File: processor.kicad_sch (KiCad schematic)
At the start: 84 parts, among them J1 Cartrige, Q1 2N3904, Q2 2N3904, Q3 2N3904, Q4 2N3904, Q5 2N3904, SW1 RESET, U1 68000, U2 27C010, U3 27C010, U39 STB, U4 74HC74, U5 LM555xM, U6 74LS05, Y1 4.433618MHz, Y2 32.084988MHz

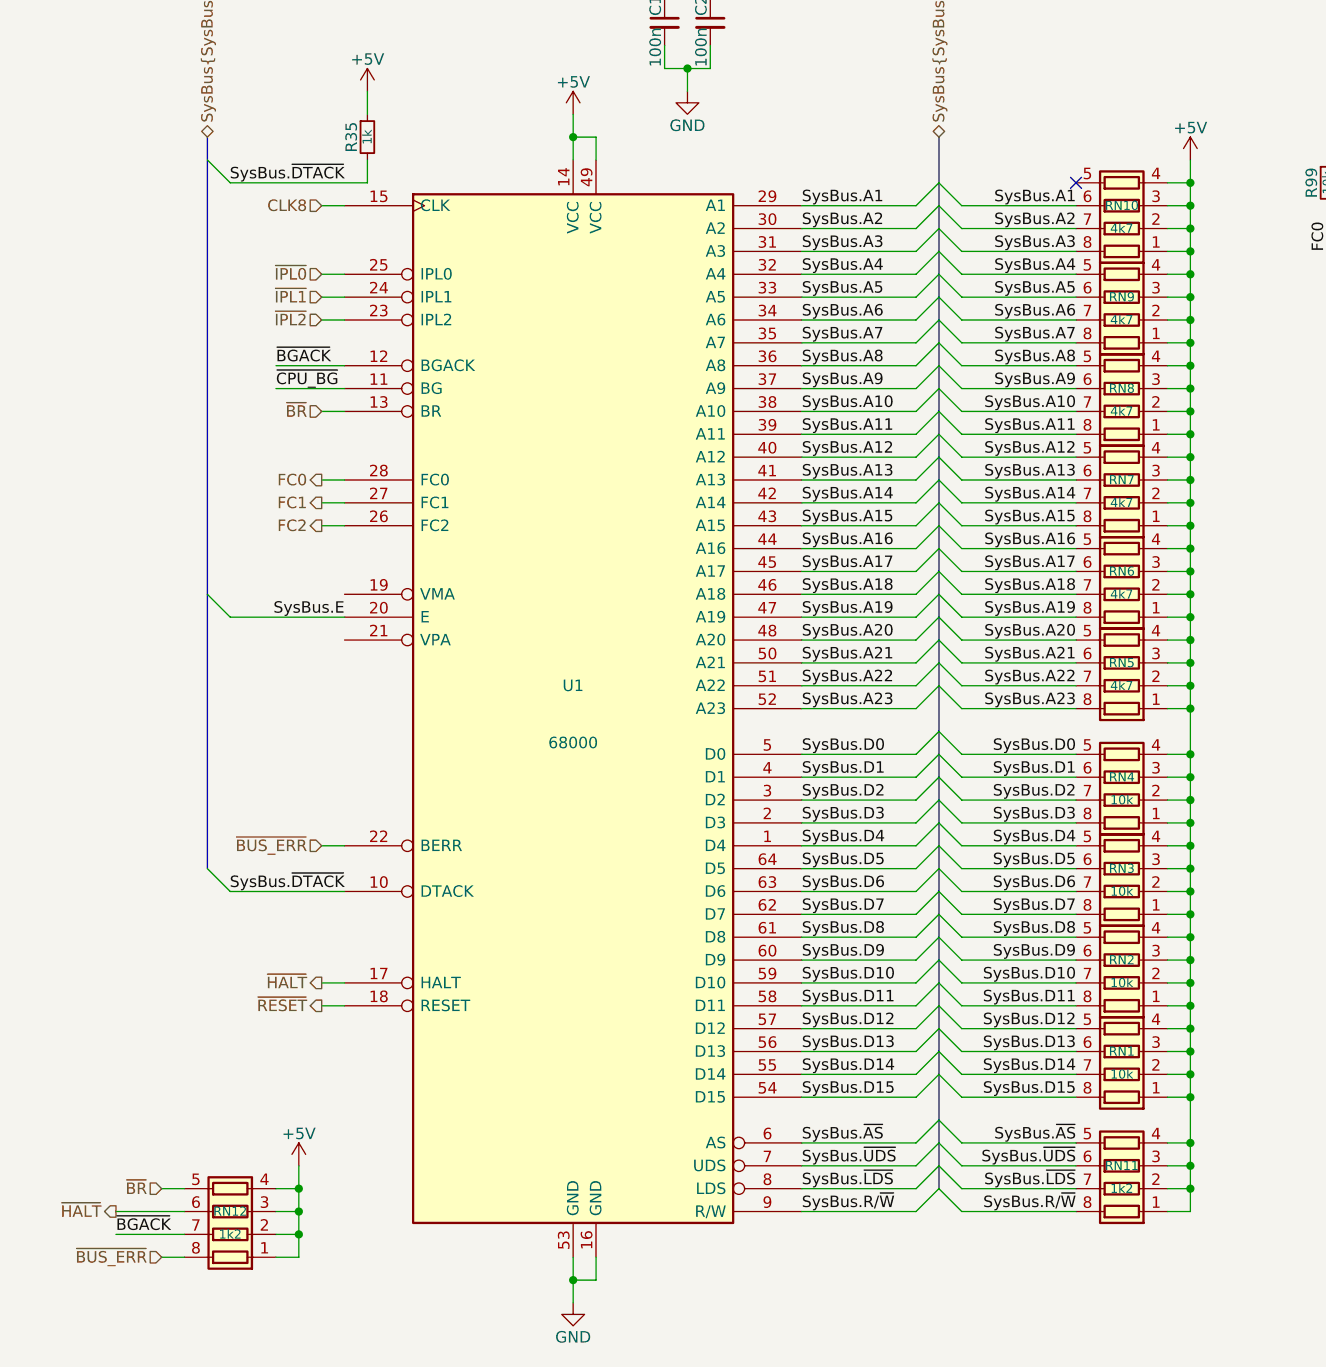
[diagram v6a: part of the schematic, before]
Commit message: motherboard: Fixed a pile of resistor network issues, and concluded initial routing of the CPU and audio amp passives
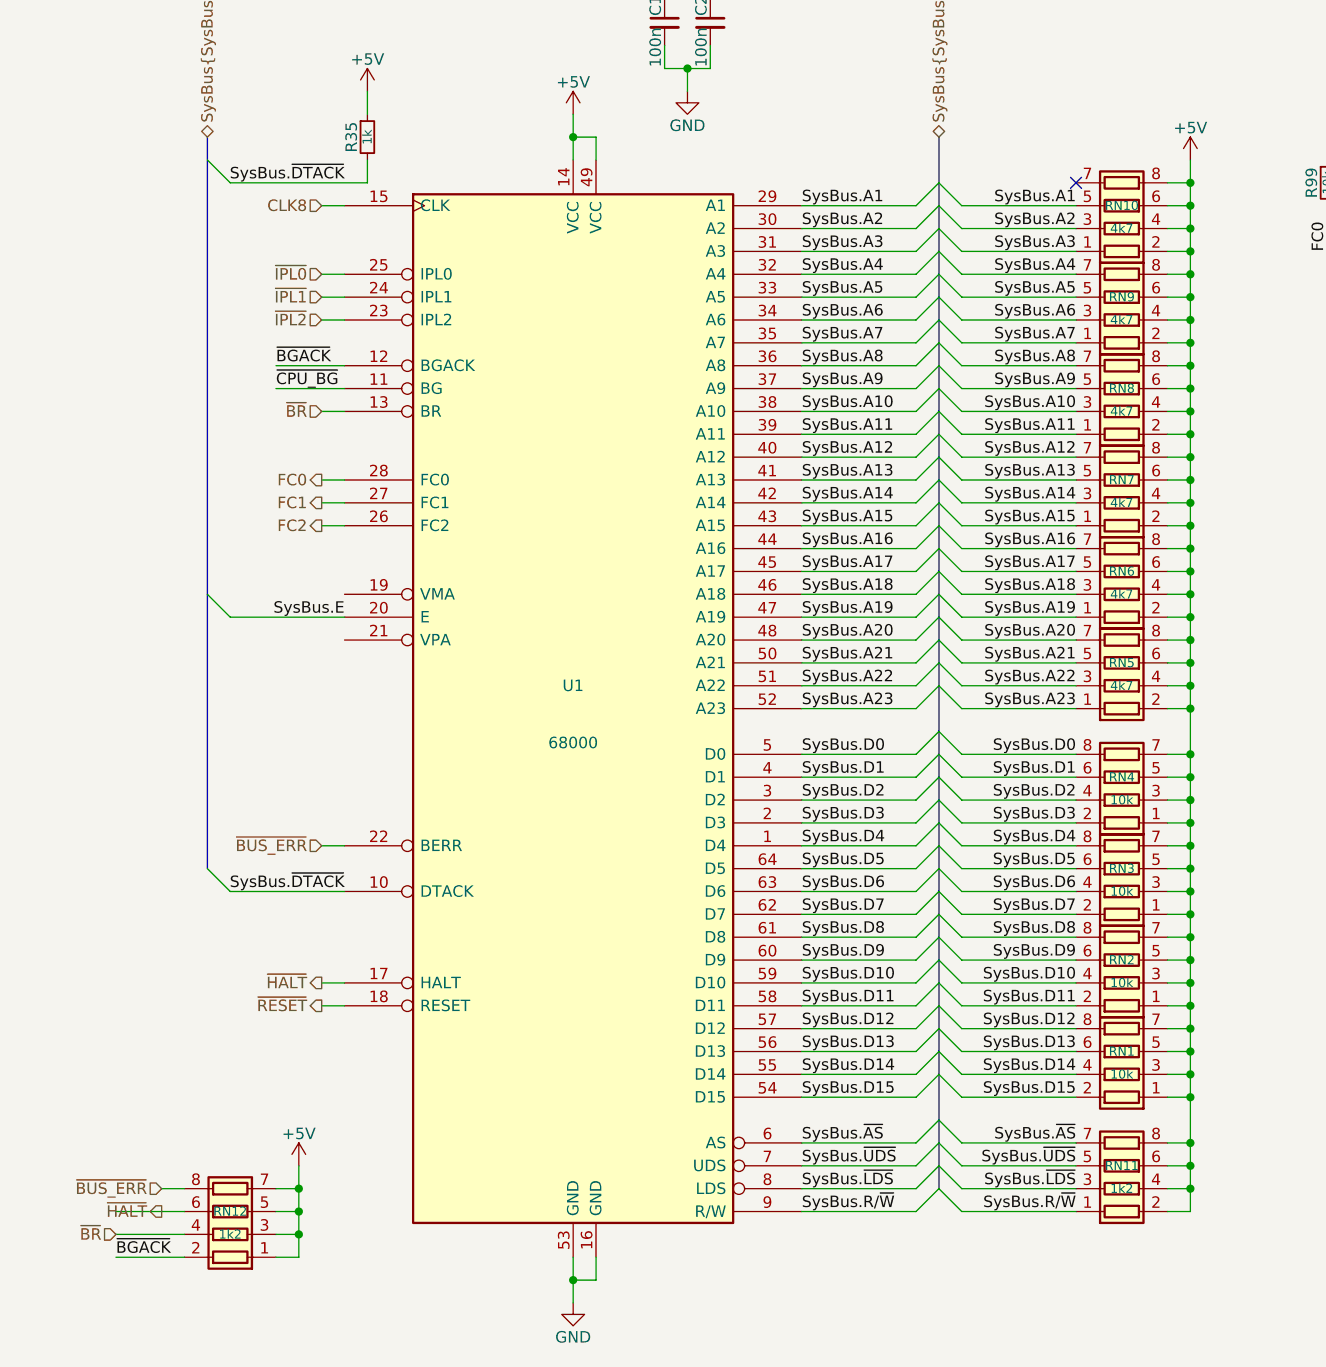
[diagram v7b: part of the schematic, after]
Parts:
- RN1, RN10, RN11, RN12, RN2, RN3, RN4, RN5, RN6, RN7, RN8, RN9: symbol Device:R_Pack04 -> dragonmux:R_Pack04_OddEven
- U1: footprint Package_DIP:DIP-64_W22.86mm_Socket -> rhais_package-dip:DIP-64_W22.86mm_Socket
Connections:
- net +5V: now also RN1.5 (R4.2), RN1.7 (R2.2), RN10.6 (R3.2), RN10.8 (R1.2), RN11.6 (R3.2), RN11.8 (R1.2), RN12.5 (R4.2), RN12.7 (R2.2), RN2.5 (R4.2), RN2.7 (R2.2), RN3.5 (R4.2), RN3.7 (R2.2), RN4.5 (R4.2), RN4.7 (R2.2), RN5.6 (R3.2), RN5.8 (R1.2), RN6.6 (R3.2), RN6.8 (R1.2), RN7.6 (R3.2), RN7.8 (R1.2), RN8.6 (R3.2), RN8.8 (R1.2), RN9.6 (R3.2), RN9.8 (R1.2); no longer RN1.2 (R2.1), RN1.4 (R4.1), RN10.1 (R1.1), RN10.3 (R3.1), RN11.1 (R1.1), RN11.3 (R3.1), RN12.2 (R2.1), RN12.4 (R4.1), RN2.2 (R2.1), RN2.4 (R4.1), RN3.2 (R2.1), RN3.4 (R4.1), RN4.2 (R2.1), RN4.4 (R4.1), RN5.1 (R1.1), RN5.3 (R3.1), RN6.1 (R1.1), RN6.3 (R3.1), RN7.1 (R1.1), RN7.3 (R3.1), RN8.1 (R1.1), RN8.3 (R3.1), RN9.1 (R1.1), RN9.3 (R3.1)
- net SysBus.A1: now also RN10.5 (R4.2); no longer RN10.6 (R3.2)
- net SysBus.A10: now also RN8.3 (R3.1); no longer RN8.7 (R2.2)
- net SysBus.A11: now also RN8.1 (R1.1); no longer RN8.8 (R1.2)
- net SysBus.A12: now also RN7.7 (R2.2); no longer RN7.5 (R4.2)
- net SysBus.A13: now also RN7.5 (R4.2); no longer RN7.6 (R3.2)
- net SysBus.A14: now also RN7.3 (R3.1); no longer RN7.7 (R2.2)
- net SysBus.A15: now also RN7.1 (R1.1); no longer RN7.8 (R1.2)
- net SysBus.A16: now also RN6.7 (R2.2); no longer RN6.5 (R4.2)
- net SysBus.A17: now also RN6.5 (R4.2); no longer RN6.6 (R3.2)
- net SysBus.A18: now also RN6.3 (R3.1); no longer RN6.7 (R2.2)
- net SysBus.A19: now also RN6.1 (R1.1); no longer RN6.8 (R1.2)
- net SysBus.A2: now also RN10.3 (R3.1); no longer RN10.7 (R2.2)
- net SysBus.A20: now also RN5.7 (R2.2); no longer RN5.5 (R4.2)
- net SysBus.A21: now also RN5.5 (R4.2); no longer RN5.6 (R3.2)
- net SysBus.A22: now also RN5.3 (R3.1); no longer RN5.7 (R2.2)
- net SysBus.A23: now also RN5.1 (R1.1); no longer RN5.8 (R1.2)
- net SysBus.A3: now also RN10.1 (R1.1); no longer RN10.8 (R1.2)
- net SysBus.A4: now also RN9.7 (R2.2); no longer RN9.5 (R4.2)
- net SysBus.A5: now also RN9.5 (R4.2); no longer RN9.6 (R3.2)
- net SysBus.A6: now also RN9.3 (R3.1); no longer RN9.7 (R2.2)
- net SysBus.A7: now also RN9.1 (R1.1); no longer RN9.8 (R1.2)
- net SysBus.A8: now also RN8.7 (R2.2); no longer RN8.5 (R4.2)
- net SysBus.A9: now also RN8.5 (R4.2); no longer RN8.6 (R3.2)
- net SysBus.D0: now also RN4.8 (R1.2); no longer RN4.5 (R4.2)
- net SysBus.D10: now also RN2.4 (R4.1); no longer RN2.7 (R2.2)
- net SysBus.D11: now also RN2.2 (R2.1); no longer RN2.8 (R1.2)
- net SysBus.D12: now also RN1.8 (R1.2); no longer RN1.5 (R4.2)
- net SysBus.D14: now also RN1.4 (R4.1); no longer RN1.7 (R2.2)
- net SysBus.D15: now also RN1.2 (R2.1); no longer RN1.8 (R1.2)
- net SysBus.D2: now also RN4.4 (R4.1); no longer RN4.7 (R2.2)
- net SysBus.D3: now also RN4.2 (R2.1); no longer RN4.8 (R1.2)
- net SysBus.D4: now also RN3.8 (R1.2); no longer RN3.5 (R4.2)
- net SysBus.D6: now also RN3.4 (R4.1); no longer RN3.7 (R2.2)
- net SysBus.D7: now also RN3.2 (R2.1); no longer RN3.8 (R1.2)
- net SysBus.D8: now also RN2.8 (R1.2); no longer RN2.5 (R4.2)
- net SysBus.R/~{W}: now also RN11.1 (R1.1); no longer RN11.8 (R1.2)
- net SysBus.~{AS}: now also RN11.7 (R2.2); no longer RN11.5 (R4.2)
- net SysBus.~{LDS}: now also RN11.3 (R3.1); no longer RN11.7 (R2.2)
- net SysBus.~{UDS}: now also RN11.5 (R4.2); no longer RN11.6 (R3.2)
- net ~{BGACK}: now also RN12.2 (R2.1); no longer RN12.7 (R2.2)
- net ~{BR}: now also RN12.4 (R4.1); no longer RN12.5 (R4.2)
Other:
- moved on the sheet: RN10, RN11, RN5, RN6, RN7, RN8, RN9
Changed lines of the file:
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@@
 	(wire
 		(pts
-			(xy 25.4 236.22) (xy 33.02 236.22)
+			(xy 25.4 238.76) (xy 33.02 238.76)
 		)
 		(stroke
@@
 	(wire
 		(pts
+			(xy 25.4 236.22) (xy 33.02 236.22)
+		)
+		(stroke
+			(width 0)
+			(type default)
+		)
+	)
+	(wire
+		(pts
 			(xy 332.74 177.8) (xy 345.44 177.8)
 		)
@@
 	(wire
 		(pts
-			(xy 30.48 238.76) (xy 33.02 238.76)
-		)
-		(stroke
-			(width 0)
-			(type default)
-		)
-	)
-	(wire
-		(pts
 			(xy 25.4 233.68) (xy 33.02 233.68)
 		)
@@
 	)
 	(label "~{BGACK}"
-		(at 25.4 236.22 0)
+		(at 25.4 238.76 0)
 		(effects
 			(font
@@
 	(hierarchical_label "~{BR}"
 		(shape input)
-		(at 30.48 231.14 180)
+		(at 25.4 236.22 180)
 		(effects
 			(font
@@
 	(hierarchical_label "~{BUS_ERR}"
 		(shape input)
-		(at 30.48 238.76 180)
+		(at 30.48 231.14 180)
 		(effects
 			(font
@@
 	(hierarchical_label "~{HALT}"
 		(shape output)
-		(at 25.4 233.68 180)
+		(at 30.48 233.68 180)
 		(effects
 			(font
@@
 			)
 		)
-		(property "Footprint" "Package_DIP:DIP-64_W22.86mm_Socket"
+		(property "Footprint" "rhais_package-dip:DIP-64_W22.86mm_Socket"
 			(at 76.2 177.8 0)
 			(effects
@@
 	)
 	(symbol
-		(lib_id "Device:R_Pack04")
+		(lib_id "dragonmux:R_Pack04_OddEven")
 		(at 137.16 195.58 90)
 		(unit 1)
@@
 		)
 		(property "Description" "4 resistor network, parallel topology"
-			(at 137.16 195.58 0)
+			(at 149.86 196.85 0)
 			(effects
 				(font
@@
 	)
 	(symbol
-		(lib_id "Device:R_Pack04")
+		(lib_id "dragonmux:R_Pack04_OddEven")
 		(at 137.16 205.74 90)
 		(unit 1)
@@
 		)
 		(property "Description" "4 resistor network, parallel topology"
-			(at 137.16 205.74 0)
+			(at 149.86 207.01 0)
 			(effects
 				(font
@@
 	)
 	(symbol
-		(lib_id "Device:R_Pack04")
-		(at 137.16 152.4 90)
+		(lib_id "dragonmux:R_Pack04_OddEven")
+		(at 137.16 152.4 270)
+		(mirror x)
 		(unit 1)
 		(exclude_from_sim no)
@@
 		)
 		(property "Description" "4 resistor network, parallel topology"
-			(at 137.16 152.4 0)
+			(at 124.46 153.67 0)
 			(effects
 				(font
@@
 	)
 	(symbol
-		(lib_id "Device:R_Pack04")
-		(at 137.16 121.92 90)
+		(lib_id "dragonmux:R_Pack04_OddEven")
+		(at 137.16 121.92 270)
+		(mirror x)
 		(unit 1)
 		(exclude_from_sim no)
@@
 		)
 		(property "Description" "4 resistor network, parallel topology"
-			(at 137.16 121.92 0)
+			(at 124.46 123.19 0)
 			(effects
 				(font
@@
 	)
 	(symbol
-		(lib_id "Device:R_Pack04")
-		(at 137.16 142.24 90)
+		(lib_id "dragonmux:R_Pack04_OddEven")
+		(at 137.16 142.24 270)
+		(mirror x)
 		(unit 1)
 		(exclude_from_sim no)
@@
 		)
 		(property "Description" "4 resistor network, parallel topology"
-			(at 137.16 142.24 0)
+			(at 124.46 143.51 0)
 			(effects
 				(font
@@
 	)
 	(symbol
-		(lib_id "Device:R_Pack04")
+		(lib_id "dragonmux:R_Pack04_OddEven")
 		(at 137.16 215.9 90)
 		(unit 1)
@@
 		)
 		(property "Description" "4 resistor network, parallel topology"
-			(at 137.16 215.9 0)
+			(at 149.86 217.17 0)
 			(effects
 				(font
@@
 	)
 	(symbol
-		(lib_id "Device:R_Pack04")
-		(at 137.16 132.08 90)
+		(lib_id "dragonmux:R_Pack04_OddEven")
+		(at 137.16 132.08 270)
+		(mirror x)
 		(unit 1)
 		(exclude_from_sim no)
@@
 		)
 		(property "Description" "4 resistor network, parallel topology"
-			(at 137.16 132.08 0)
+			(at 124.46 133.35 0)
 			(effects
 				(font
@@
 	)
 	(symbol
-		(lib_id "Device:R_Pack04")
+		(lib_id "dragonmux:R_Pack04_OddEven")
 		(at 38.1 233.68 90)
 		(unit 1)
@@
 		)
 		(property "Description" "4 resistor network, parallel topology"
-			(at 38.1 233.68 0)
+			(at 50.8 234.95 0)
 			(effects
 				(font
@@
 	)
 	(symbol
-		(lib_id "Device:R_Pack04")
+		(lib_id "dragonmux:R_Pack04_OddEven")
 		(at 137.16 185.42 90)
 		(unit 1)
@@
 		)
 		(property "Description" "4 resistor network, parallel topology"
-			(at 137.16 185.42 0)
+			(at 149.86 186.69 0)
 			(effects
 				(font
@@
 	)
 	(symbol
-		(lib_id "Device:R_Pack04")
-		(at 137.16 228.6 90)
+		(lib_id "dragonmux:R_Pack04_OddEven")
+		(at 137.16 228.6 270)
+		(mirror x)
 		(unit 1)
 		(exclude_from_sim no)
@@
 		)
 		(property "Description" "4 resistor network, parallel topology"
-			(at 137.16 228.6 0)
+			(at 124.46 229.87 0)
 			(effects
 				(font
@@
 	)
 	(symbol
-		(lib_id "Device:R_Pack04")
-		(at 137.16 172.72 90)
+		(lib_id "dragonmux:R_Pack04_OddEven")
+		(at 137.16 172.72 270)
+		(mirror x)
 		(unit 1)
 		(exclude_from_sim no)
@@
 		)
 		(property "Description" "4 resistor network, parallel topology"
-			(at 137.16 172.72 0)
+			(at 124.46 173.99 0)
 			(effects
 				(font
@@
 	)
 	(symbol
-		(lib_id "Device:R_Pack04")
-		(at 137.16 162.56 90)
+		(lib_id "dragonmux:R_Pack04_OddEven")
+		(at 137.16 162.56 270)
+		(mirror x)
 		(unit 1)
 		(exclude_from_sim no)
@@
 		)
 		(property "Description" "4 resistor network, parallel topology"
-			(at 137.16 162.56 0)
+			(at 124.46 163.83 0)
 			(effects
 				(font

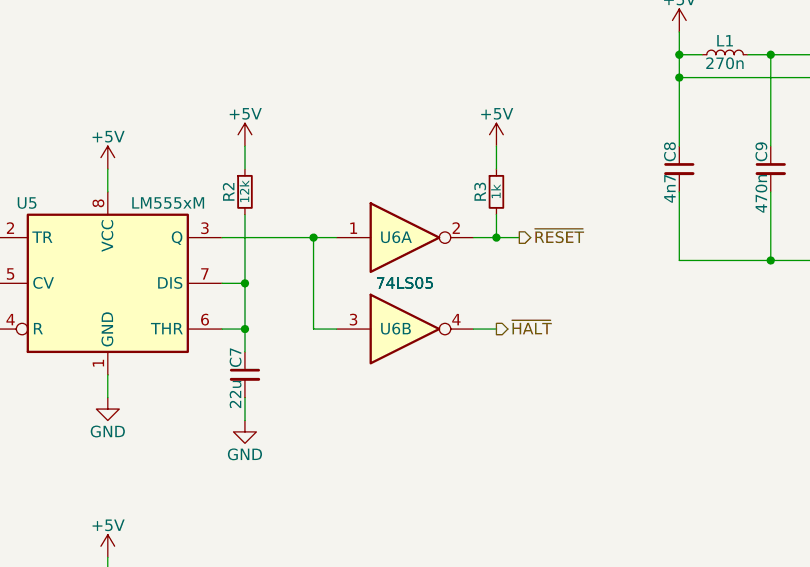
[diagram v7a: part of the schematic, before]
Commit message: motherboard: Added packaging and ordering information for many of the 7400 logic parts and the DACs
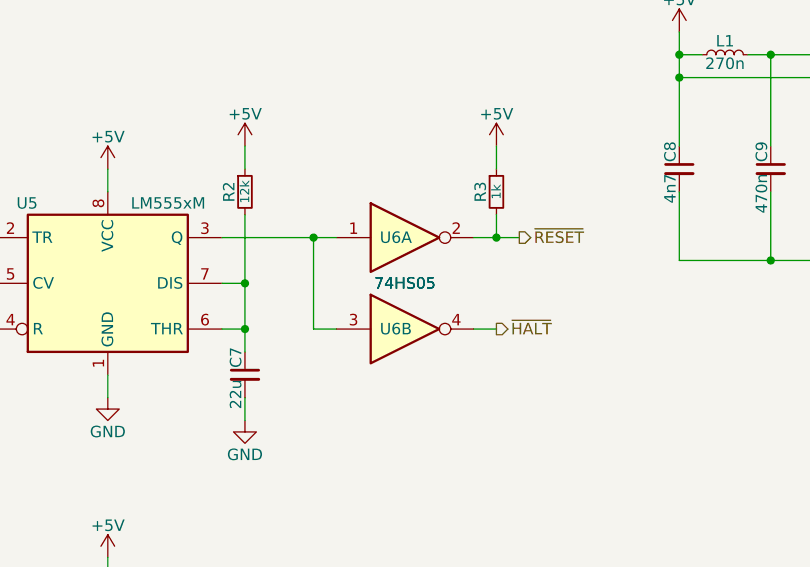
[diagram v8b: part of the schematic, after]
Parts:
- U4: footprint (none) -> rhais_package-smd:SO-14_3.9x8.65mm_P1.27mm; symbol 74xx:74HC74 -> 74xx:74LS74; MFR (none) -> Nexperia; MPN (none) -> 74HC74D,653; OC_FARNELL (none) -> 1201317
- U4: footprint (none) -> rhais_package-smd:SO-14_3.9x8.65mm_P1.27mm; MFR (none) -> Nexperia; MPN (none) -> 74HC74D,653; OC_FARNELL (none) -> 1201317
- U6: value 74LS05 -> 74HS05
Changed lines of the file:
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@@
 	)
 	(symbol
-		(lib_id "74xx:74HC74")
+		(lib_id "74xx:74LS74")
 		(at 259.08 50.8 0)
 		(unit 2)
@@
 			)
 		)
-		(property "Footprint" ""
+		(property "Footprint" "rhais_package-smd:SO-14_3.9x8.65mm_P1.27mm"
 			(at 259.08 50.8 0)
 			(effects
@@
 			)
 		)
-		(property "Datasheet" "74xx/74hc_hct74.pdf"
+		(property "Datasheet" "https://assets.nexperia.com/documents/data-sheet/74HC_HCT74.pdf"
 			(at 259.08 50.8 0)
 			(effects
@@
 			)
 		)
-		(property "MFR" ""
+		(property "MFR" "Nexperia"
 			(at 259.08 50.8 0)
 			(effects
@@
 			)
 		)
-		(property "MPN" ""
+		(property "MPN" "74HC74D,653"
 			(at 259.08 50.8 0)
 			(effects
@@
 			)
 		)
-		(property "OC_FARNELL" ""
+		(property "OC_FARNELL" "1201317"
 			(at 259.08 50.8 0)
 			(effects
@@
 			)
 		)
-		(property "Footprint" ""
+		(property "Footprint" "rhais_package-smd:SO-14_3.9x8.65mm_P1.27mm"
 			(at 127 -12.7 0)
 			(effects
@@
 			)
 		)
-		(property "Datasheet" "74xx/74hc_hct74.pdf"
+		(property "Datasheet" "https://assets.nexperia.com/documents/data-sheet/74HC_HCT74.pdf"
 			(at 127 -12.7 0)
 			(effects
@@
 			)
 		)
-		(property "MFR" ""
+		(property "MFR" "Nexperia"
 			(at 127 -12.7 0)
 			(effects
@@
 			)
 		)
-		(property "MPN" ""
+		(property "MPN" "74HC74D,653"
 			(at 127 -12.7 0)
 			(effects
@@
 			)
 		)
-		(property "OC_FARNELL" ""
+		(property "OC_FARNELL" "1201317"
 			(at 127 -12.7 0)
 			(effects
@@
 			)
 		)
-		(property "Value" "74LS05"
+		(property "Value" "74HS05"
 			(at 121.92 63.5 0)
 			(effects
@@
 			)
 		)
-		(property "Value" "74LS05"
+		(property "Value" "74HS05"
 			(at 121.92 63.5 0)
 			(effects
@@
 			)
 		)
-		(property "Footprint" ""
+		(property "Footprint" "rhais_package-smd:SO-14_3.9x8.65mm_P1.27mm"
 			(at 179.07 -12.7 0)
 			(effects
@@
 			)
 		)
-		(property "Datasheet" "74xx/74hc_hct74.pdf"
+		(property "Datasheet" "https://assets.nexperia.com/documents/data-sheet/74HC_HCT74.pdf"
 			(at 179.07 -12.7 0)
 			(effects
@@
 			)
 		)
-		(property "MFR" ""
+		(property "MFR" "Nexperia"
 			(at 179.07 -12.7 0)
 			(effects
@@
 			)
 		)
-		(property "MPN" ""
+		(property "MPN" "74HC74D,653"
 			(at 179.07 -12.7 0)
 			(effects
@@
 			)
 		)
-		(property "OC_FARNELL" ""
+		(property "OC_FARNELL" "1201317"
 			(at 179.07 -12.7 0)
 			(effects
